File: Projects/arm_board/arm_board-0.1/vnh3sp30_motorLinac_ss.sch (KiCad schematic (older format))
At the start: 3 parts

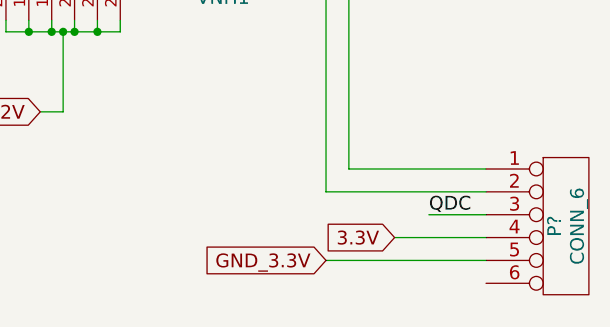
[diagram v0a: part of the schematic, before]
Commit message: Arm Board: Finish schematic
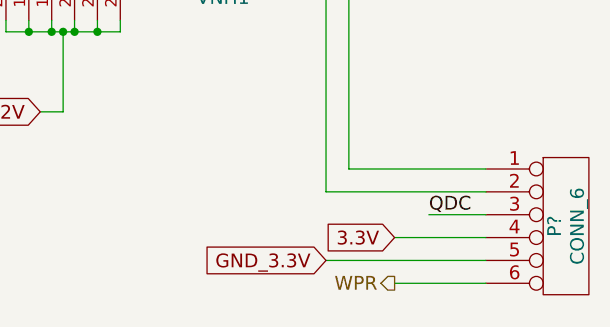
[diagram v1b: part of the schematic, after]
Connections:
- net WPR: now reaches P?.6
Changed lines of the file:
@@
 $Descr A4 11693 8268
 encoding utf-8
-Sheet 6 23
+Sheet 21 23
 Title ""
 Date "14 jan 2016"
@@
 AR Path="/56F5245F/564A6239" Ref="VNH1"  Part="1"
 AR Path="/56F544AF/564A6239" Ref="VNH1"  Part="1"
+AR Path="/56F75F1F/564A6239" Ref="VNH1"  Part="1"
 F 0 "VNH1" H 9250 2850 60  0000 C CNN
 F 1 "VNH3SP30" H 8550 3800 60  0000 C CNN
@@
 AR Path="/56F5245F/565DD202" Ref="U?"  Part="1"
 AR Path="/56F544AF/565DD202" Ref="U?"  Part="1"
+AR Path="/56F75F1F/565DD202" Ref="U?"  Part="1"
 F 0 "U?" H 4750 4450 60  0000 C CNN
 F 1 "74LVC2G08" V 4500 4900 60  0000 C CNN
@@
 AR Path="/56F5245F/56F466A7" Ref="P?"  Part="1"
 AR Path="/56F544AF/56F466A7" Ref="P?"  Part="1"
+AR Path="/56F75F1F/56F466A7" Ref="P?"  Part="1"
 F 0 "P?" V 10700 5750 60  0000 C CNN
 F 1 "CONN_6" V 10800 5750 60  0000 C CNN
@@
 Wire Wire Line
 	9700 4050 9400 4050
+Text HLabel 10000 6000 0    60   Output ~ 0
+WPR
+Wire Wire Line
+	10000 6000 10400 6000
 $EndSCHEMATC

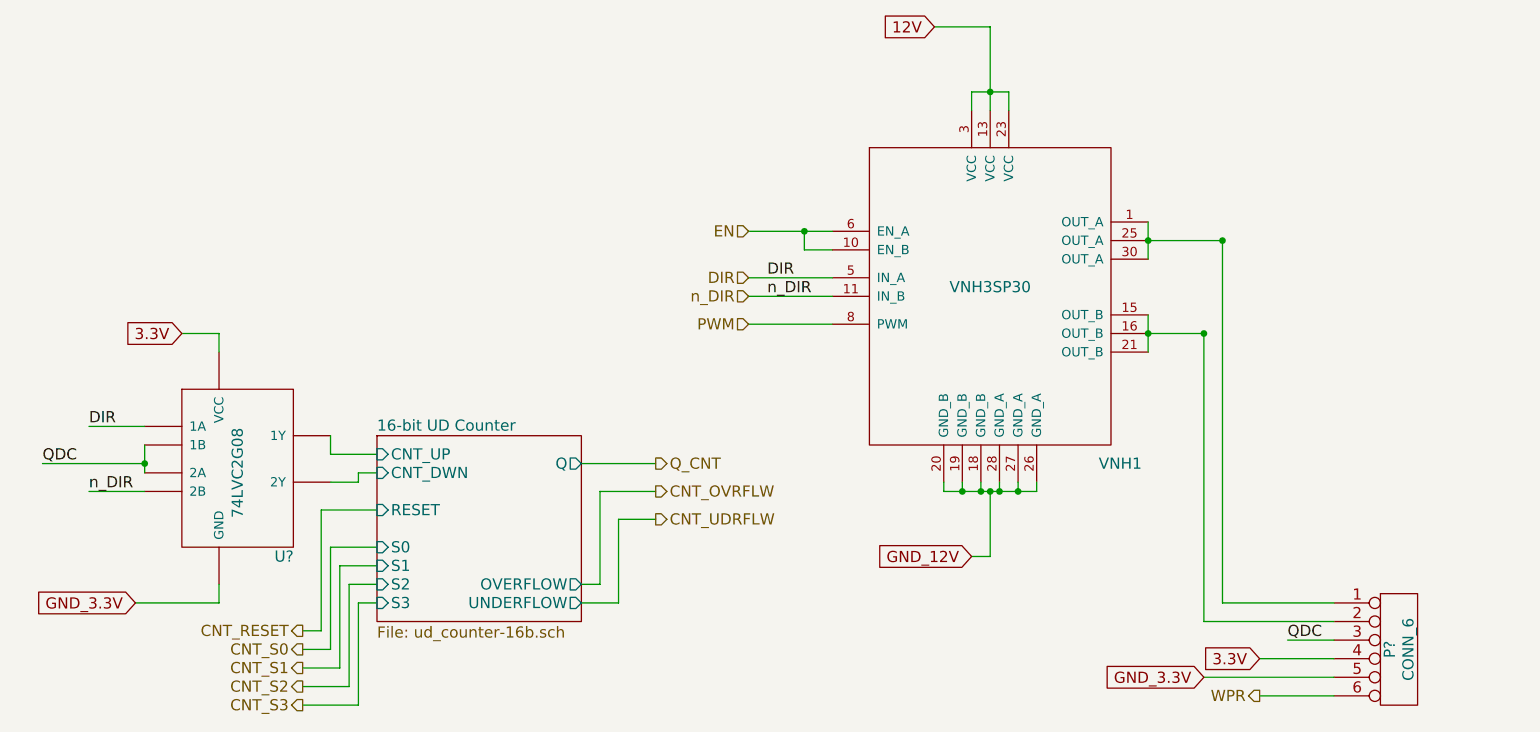
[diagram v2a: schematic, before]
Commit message: Arm Board: bug fixes, and added footprints
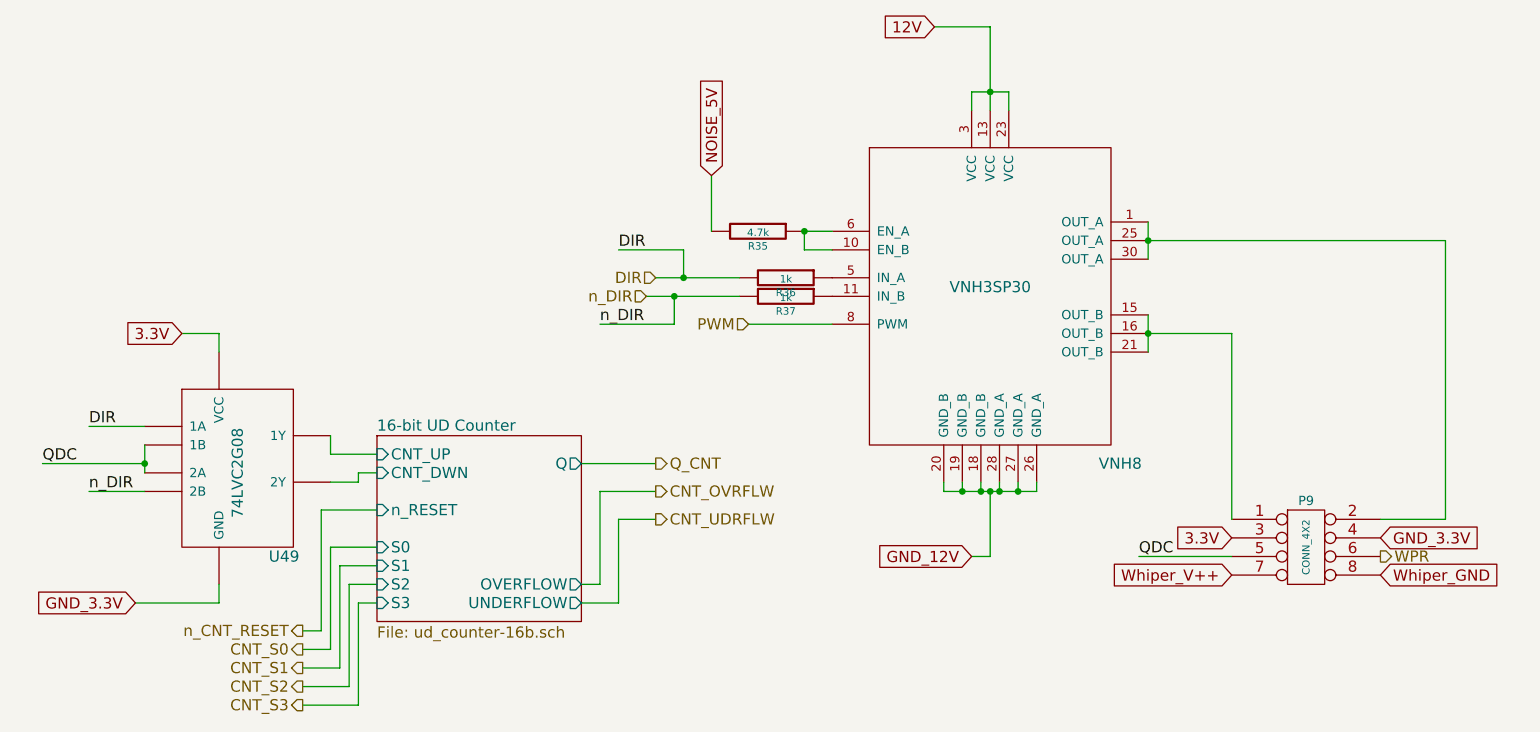
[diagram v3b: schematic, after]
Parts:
- removed P?: CONN_6, ~, symbol CONN_6
- removed U?: 74LVC2G08, symbol 74LVC2G08
- removed VNH1: VNH3SP30, symbol VNH3SP30
- added P9: CONN_4X2, ArmFootprints:MiniFitJr_8-pin_0050348563, symbol CONN_4X2
- added R35: 4.7k, Resistors_SMD:R_0805, symbol R
- added R36, R37: 1k, Resistors_SMD:R_0805, symbol R
- added U49: 74LVC2G08, ArmFootprints:SN74LVC2G08DCTR, symbol 74LVC2G08
- added VNH8: VNH3SP30, ArmFootprints:VNH3SP30TR-E, symbol VNH3SP30
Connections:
- net 12V: now also VNH8.13 (VCC), VNH8.23 (VCC), VNH8.3 (VCC)
- net 16-bit UD Counter/CNT_DWN: now also U49.~ (VCC)
- net 16-bit UD Counter/CNT_UP: now also U49.~ (VCC)
- net 3.3V: now also P9.3, U49.~ (VCC)
- net DIR: now also R36.2, U49.~ (VCC)
- net GND_12V: now also VNH8.18 (GND_B), VNH8.19 (GND_B), VNH8.20 (GND_B), VNH8.26 (GND_A), VNH8.27 (GND_A), VNH8.28 (GND_A)
- net GND_3.3V: now also P9.4, U49.~ (VCC)
- net PWM: now also VNH8.8 (PWM)
- net QDC: now also P9.5, U49.~ (VCC)
- net WPR: now also P9.6
- net n_DIR: now also R37.2, U49.~ (VCC)
- new net: P9.2, VNH8.1 (OUT_A), VNH8.25 (OUT_A), VNH8.30 (OUT_A)
- new net: R35.1, VNH8.10 (EN_B), VNH8.6 (EN_A)
- new net: R37.1, VNH8.11 (IN_B)
- new net: P9.1, VNH8.15 (OUT_B), VNH8.16 (OUT_B), VNH8.21 (OUT_B)
- new net: R36.1, VNH8.5 (IN_A)
- new net NOISE_5V: R35.2
- new net Whiper_GND: P9.8
- new net Whiper_V++: P9.7
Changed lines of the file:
@@
 LIBS:ArmComponentLibrary
 LIBS:arm_board-cache
-EELAYER 27 0
+EELAYER 25 0
 EELAYER END
 $Descr A4 11693 8268
 encoding utf-8
-Sheet 21 23
+Sheet 18 23
 Title ""
 Date "30 jan 2016"
@@
 $EndDescr
 $Comp
-L VNH3SP30 VNH1
-U 1 1 564A6239
+L VNH3SP30 VNH8
+U 1 1 56AED672
 P 8550 3800
-AR Path="/564B31DF/564A6239" Ref="VNH1"  Part="1"
-AR Path="/56666F75/564A6239" Ref="VNH1"  Part="1"
-AR Path="/56669634/564A6239" Ref="VNH1"  Part="1"
-AR Path="/56669644/564A6239" Ref="VNH1"  Part="1"
-AR Path="/5666D2E0/564A6239" Ref="VNH1"  Part="1"
-AR Path="/5666D2F0/564A6239" Ref="VNH1"  Part="1"
-AR Path="/56F5245F/564A6239" Ref="VNH1"  Part="1"
-AR Path="/56F544AF/564A6239" Ref="VNH1"  Part="1"
-AR Path="/56F75F1F/564A6239" Ref="VNH1"  Part="1"
-F 0 "VNH1" H 9250 2850 60  0000 C CNN
+F 0 "VNH8" H 9250 2850 60  0000 C CNN
 F 1 "VNH3SP30" H 8550 3800 60  0000 C CNN
-F 2 "" H 6950 3600 60  0000 C CNN
+F 2 "ArmFootprints:VNH3SP30TR-E" H 6950 3600 60  0001 C CNN
 F 3 "" H 6950 3600 60  0000 C CNN
 	1    8550 3800
@@
 	8550 5250 8550 4900
 Connection ~ 8550 4900
-Text HLabel 7250 3750 0    60   Input ~ 0
+Text HLabel 6750 3750 0    60   Input ~ 0
 DIR
-Text HLabel 7250 3850 0    60   Input ~ 0
+Text HLabel 6700 3850 0    60   Input ~ 0
 n_DIR
 Text HLabel 7250 4000 0    60   Input ~ 0
@@
 Wire Wire Line
 	7250 4000 7700 4000
-Wire Wire Line
-	7250 3850 7700 3850
-Wire Wire Line
-	7250 3750 7700 3750
-Wire Wire Line
-	7250 3500 7700 3500
 $Sheet
 S 5250 4600 1100 1000
-U 564A908F
+U 56AED673
 F0 "16-bit UD Counter" 60
 F1 "ud_counter-16b.sch" 60
@@
 F5 "CNT_UP" I L 5250 4700 60
 F6 "CNT_DWN" I L 5250 4800 60
-F7 "RESET" I L 5250 5000 60
-F8 "S0" I L 5250 5200 60
-F9 "S1" I L 5250 5300 60
-F10 "S2" I L 5250 5400 60
-F11 "S3" I L 5250 5500 60
+F7 "S0" I L 5250 5200 60
+F8 "S1" I L 5250 5300 60
+F9 "S2" I L 5250 5400 60
+F10 "S3" I L 5250 5500 60
+F11 "n_RESET" I L 5250 5000 60
 $EndSheet
-Wire Wire Line
-	7700 3600 7550 3600
-Wire Wire Line
-	7550 3600 7550 3500
-Connection ~ 7550 3500
-Text HLabel 7250 3500 0    60   Input ~ 0
-EN
-Text Label 7350 3750 0    60   ~ 0
+Text Label 6550 3600 0    60   ~ 0
 DIR
-Text Label 7350 3850 0    60   ~ 0
+Text Label 6450 4000 0    60   ~ 0
 n_DIR
 $Comp
-L 74LVC2G08 U?
-U 1 1 565DD202
+L 74LVC2G08 U49
+U 1 1 56AED674
 P 4650 4850
-AR Path="/564B31DF/565DD202" Ref="U?"  Part="1"
-AR Path="/56666F75/565DD202" Ref="U?"  Part="1"
-AR Path="/56669634/565DD202" Ref="U?"  Part="1"
-AR Path="/56669644/565DD202" Ref="U?"  Part="1"
-AR Path="/5666D2E0/565DD202" Ref="U?"  Part="1"
-AR Path="/5666D2F0/565DD202" Ref="U?"  Part="1"
-AR Path="/56F5245F/565DD202" Ref="U?"  Part="1"
-AR Path="/56F544AF/565DD202" Ref="U?"  Part="1"
-AR Path="/56F75F1F/565DD202" Ref="U?"  Part="1"
-F 0 "U?" H 4750 4450 60  0000 C CNN
+F 0 "U49" H 4750 4450 60  0000 C CNN
 F 1 "74LVC2G08" V 4500 4900 60  0000 C CNN
-F 2 "" H 4650 4850 60  0000 C CNN
+F 2 "ArmFootprints:SN74LVC2G08DCTR" H 4650 4850 60  0001 C CNN
 F 3 "" H 4650 4850 60  0000 C CNN
 	1    4650 4850
@@
 CNT_UDRFLW
 Text HLabel 4850 5650 0    60   Output ~ 0
-CNT_RESET
+n_CNT_RESET
 Text HLabel 4850 5750 0    60   Output ~ 0
 CNT_S0
@@
 	9400 3950 9400 4150
 Connection ~ 9400 4050
-$Comp
-L CONN_6 P?
-U 1 1 56F466A7
-P 10750 5750
-AR Path="/564B31DF/56F466A7" Ref="P?"  Part="1"
-AR Path="/56F5245F/56F466A7" Ref="P?"  Part="1"
-AR Path="/56F544AF/56F466A7" Ref="P?"  Part="1"
-AR Path="/56F75F1F/56F466A7" Ref="P?"  Part="1"
-F 0 "P?" V 10700 5750 60  0000 C CNN
-F 1 "CONN_6" V 10800 5750 60  0000 C CNN
-F 2 "~" H 10750 5750 60  0000 C CNN
-F 3 "~" H 10750 5750 60  0000 C CNN
-	1    10750 5750
+Text Label 9350 5250 0    60   ~ 0
+QDC
+Text GLabel 9850 5350 0    60   Input ~ 0
+Whiper_V++
+Wire Wire Line
+	9400 3550 11000 3550
+Text HLabel 10650 5250 2    60   Output ~ 0
+WPR
+Text GLabel 10650 5350 2    60   Input ~ 0
+Whiper_GND
+$Comp
+L R R36
+U 1 1 56C6163E
+P 7450 3750
+F 0 "R36" V 7530 3750 40  0000 C CNN
+F 1 "1k" V 7457 3751 40  0000 C CNN
+F 2 "Resistors_SMD:R_0805" V 7380 3750 30  0001 C CNN
+F 3 "" H 7450 3750 30  0000 C CNN
+	1    7450 3750
+	0    1    1    0
+$EndComp
+Wire Wire Line
+	7200 3750 6750 3750
+Wire Wire Line
+	6550 3600 6900 3600
+Wire Wire Line
+	6900 3600 6900 3750
+Connection ~ 6900 3750
+$Comp
+L R R37
+U 1 1 56C618B9
+P 7450 3850
+F 0 "R37" V 7530 3850 40  0000 C CNN
+F 1 "1k" V 7457 3851 40  0000 C CNN
+F 2 "Resistors_SMD:R_0805" V 7380 3850 30  0001 C CNN
+F 3 "" H 7450 3850 30  0000 C CNN
+	1    7450 3850
+	0    1    1    0
+$EndComp
+Wire Wire Line
+	7200 3850 6700 3850
+Wire Wire Line
+	6450 4000 6850 4000
+Wire Wire Line
+	6850 4000 6850 3850
+Connection ~ 6850 3850
+Text GLabel 7050 3200 1    60   Input ~ 0
+NOISE_5V
+Connection ~ 7550 3500
+Wire Wire Line
+	7550 3600 7550 3500
+Wire Wire Line
+	7700 3600 7550 3600
+Wire Wire Line
+	7550 3500 7700 3500
+$Comp
+L R R35
+U 1 1 56C65444
+P 7300 3500
+F 0 "R35" V 7380 3500 40  0000 C CNN
+F 1 "4.7k" V 7307 3501 40  0000 C CNN
+F 2 "Resistors_SMD:R_0805" V 7230 3500 30  0001 C CNN
+F 3 "" H 7300 3500 30  0000 C CNN
+	1    7300 3500
+	0    1    1    0
+$EndComp
+Wire Wire Line
+	7050 3200 7050 3500
+Text GLabel 9850 5150 0    60   Input ~ 0
+3.3V
+Text GLabel 10650 5150 2    60   Input ~ 0
+GND_3.3V
+$Comp
+L CONN_4X2 P9
+U 1 1 56C67526
+P 10250 5200
+F 0 "P9" H 10250 5450 50  0000 C CNN
+F 1 "CONN_4X2" V 10250 5200 40  0000 C CNN
+F 2 "ArmFootprints:MiniFitJr_8-pin_0050348563" H 10250 5200 60  0001 C CNN
+F 3 "" H 10250 5200 60  0000 C CNN
+	1    10250 5200
 	1    0    0    -1
 $EndComp
 Wire Wire Line
-	9800 3550 9800 5500
-Wire Wire Line
-	9800 5500 10400 5500
-Connection ~ 9800 3550
-Wire Wire Line
-	9700 4050 9700 5600
-Wire Wire Line
-	9700 5600 10400 5600
-Connection ~ 9700 4050
-Text Label 10150 5700 0    60   ~ 0
-QDC
-Wire Wire Line
-	10150 5700 10400 5700
-Text GLabel 10000 5800 0    60   Input ~ 0
-3.3V
-Wire Wire Line
-	10000 5800 10400 5800
-Text GLabel 9700 5900 0    60   Input ~ 0
-GND_3.3V
-Wire Wire Line
-	9700 5900 10400 5900
-Wire Wire Line
-	9400 3550 9800 3550
-Wire Wire Line
-	9700 4050 9400 4050
-Text HLabel 10000 6000 0    60   Output ~ 0
-WPR
-Wire Wire Line
-	10000 6000 10400 6000
+	9850 4050 9850 5050
+Wire Wire Line
+	9350 5250 9850 5250
+Wire Wire Line
+	9400 4050 9850 4050
+Wire Wire Line
+	11000 3550 11000 5050
+Wire Wire Line
+	11000 5050 10650 5050
 $EndSCHEMATC

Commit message: Arm Board: bug fixes, cleanup, and start PCB layout
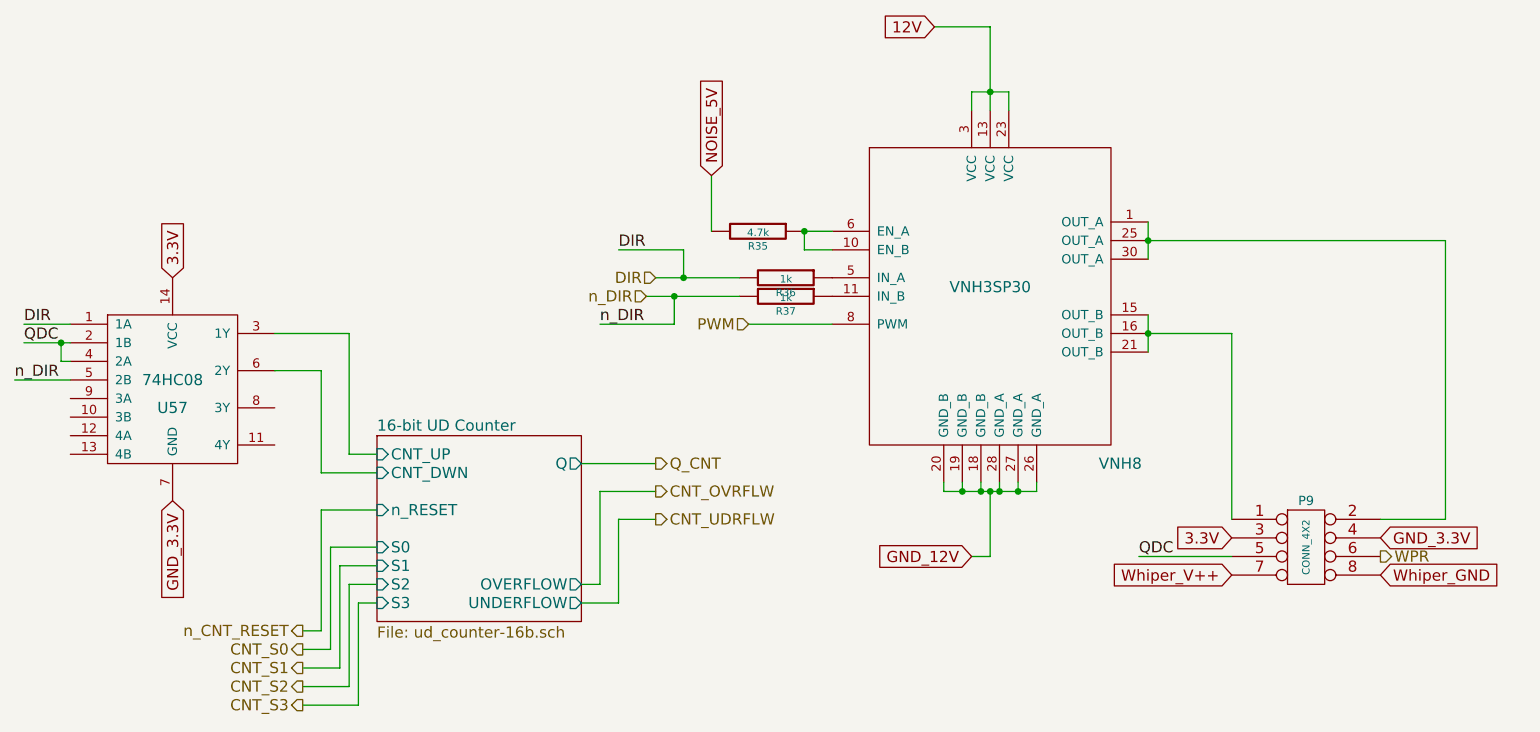
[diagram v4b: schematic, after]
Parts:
- removed U49: 74LVC2G08, ArmFootprints:SN74LVC2G08DCTR, symbol 74LVC2G08
- added U57: 74HC08, SMD_Packages:SOIC-14_N, symbol 74HC08
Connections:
- net 16-bit UD Counter/CNT_DWN: now also U57.6 (2Y)
- net 16-bit UD Counter/CNT_UP: now also U57.3 (1Y)
- net 3.3V: now also U57.14 (VCC)
- net DIR: now also U57.1 (1A)
- net GND_3.3V: now also U57.7 (GND)
- net QDC: now also U57.2 (1B), U57.4 (2A)
- net n_DIR: now also U57.5 (2B)
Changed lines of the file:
@@
 Text Label 6450 4000 0    60   ~ 0
 n_DIR
-$Comp
-L 74LVC2G08 U49
-U 1 1 56AED674
-P 4650 4850
-F 0 "U49" H 4750 4450 60  0000 C CNN
-F 1 "74LVC2G08" V 4500 4900 60  0000 C CNN
-F 2 "ArmFootprints:SN74LVC2G08DCTR" H 4650 4850 60  0001 C CNN
-F 3 "" H 4650 4850 60  0000 C CNN
-	1    4650 4850
-	1    0    0    -1
-$EndComp
-Text Label 3450 4750 0    60   ~ 0
-QDC
-Wire Wire Line
-	3450 4750 4000 4750
-Wire Wire Line
-	4000 4650 4000 4800
-Connection ~ 4000 4750
-Text Label 3700 4550 0    60   ~ 0
-DIR
-Text Label 3700 4900 0    60   ~ 0
-n_DIR
-Wire Wire Line
-	3700 4900 4000 4900
-Wire Wire Line
-	4000 4550 3700 4550
-Text GLabel 4200 4050 0    60   Input ~ 0
+Text GLabel 4150 3750 1    60   Input ~ 0
 3.3V
-Wire Wire Line
-	4200 4050 4400 4050
-Wire Wire Line
-	4400 4050 4400 4150
-Text GLabel 3950 5500 0    60   Input ~ 0
+Text GLabel 4150 4950 3    60   Input ~ 0
 GND_3.3V
-Wire Wire Line
-	3950 5500 4400 5500
-Wire Wire Line
-	4400 5500 4400 5400
-Wire Wire Line
-	5000 4600 5000 4700
-Wire Wire Line
-	5000 4700 5250 4700
-Wire Wire Line
-	5000 4850 5150 4850
-Wire Wire Line
-	5150 4850 5150 4800
-Wire Wire Line
-	5150 4800 5250 4800
 Text HLabel 6750 4750 2    60   Output ~ 0
 Q_CNT
@@
 $EndComp
 Wire Wire Line
-	7200 3750 6750 3750
+	6750 3750 7200 3750
 Wire Wire Line
 	6550 3600 6900 3600
@@
 $EndComp
 Wire Wire Line
-	7200 3850 6700 3850
+	6700 3850 7200 3850
 Wire Wire Line
 	6450 4000 6850 4000
@@
 Wire Wire Line
 	11000 5050 10650 5050
+$Comp
+L 74HC08 U57
+U 1 1 56CE788A
+P 4150 4300
+F 0 "U57" H 4150 4150 60  0000 C CNN
+F 1 "74HC08" H 4150 4300 60  0000 C CNN
+F 2 "SMD_Packages:SOIC-14_N" H 4150 4300 60  0001 C CNN
+F 3 "" H 4150 4300 60  0000 C CNN
+	1    4150 4300
+	1    0    0    -1
+$EndComp
+Text Label 3350 4100 0    60   ~ 0
+QDC
+Text Label 3350 4000 0    60   ~ 0
+DIR
+Text Label 3300 4300 0    60   ~ 0
+n_DIR
+Wire Wire Line
+	3350 4000 3600 4000
+Wire Wire Line
+	3350 4100 3600 4100
+Wire Wire Line
+	3550 4100 3550 4200
+Wire Wire Line
+	3550 4200 3600 4200
+Connection ~ 3550 4100
+Wire Wire Line
+	3300 4300 3600 4300
+Wire Wire Line
+	4700 4050 5100 4050
+Wire Wire Line
+	5100 4050 5100 4700
+Wire Wire Line
+	5100 4700 5250 4700
+Wire Wire Line
+	4700 4250 4950 4250
+Wire Wire Line
+	4950 4250 4950 4800
+Wire Wire Line
+	4950 4800 5250 4800
 $EndSCHEMATC
